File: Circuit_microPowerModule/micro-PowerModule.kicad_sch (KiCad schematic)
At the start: 5 parts, among them Q1 S8550, SW1 RotaryEncoder_Switch, U2 MAX485E

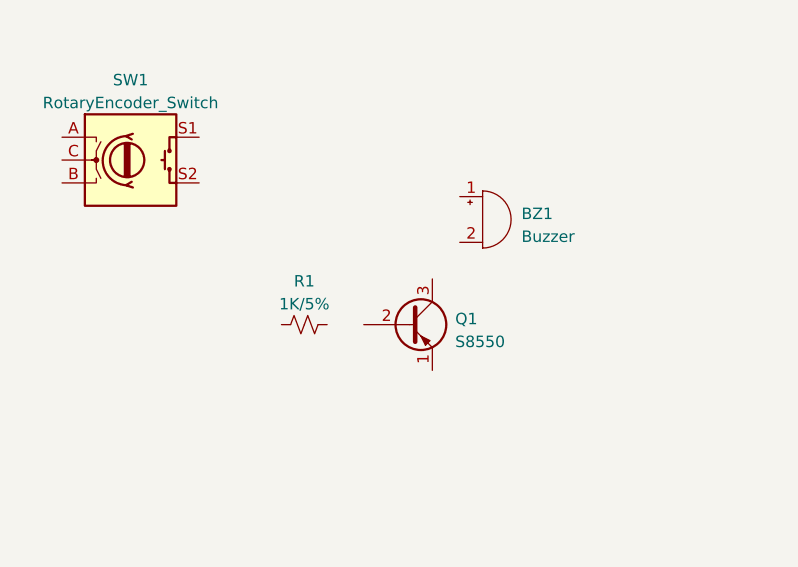
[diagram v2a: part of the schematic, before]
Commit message: new RFQ, update circuit
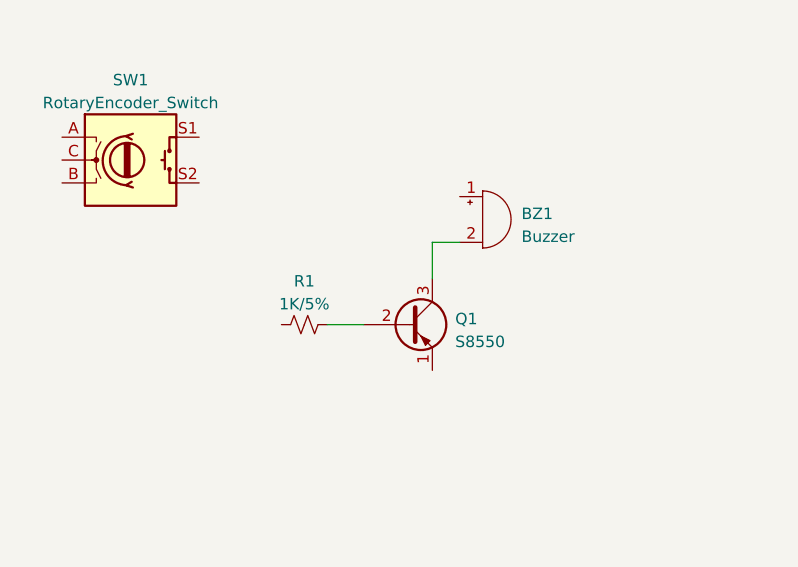
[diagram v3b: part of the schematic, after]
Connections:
- net at Q1.2 (B): now also R1.2
- net at Q1.3 (C): now also BZ1.2 (+)
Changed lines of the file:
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@@
     (rev "0.0")
+  )
+  (wire (pts (xy 98.552 146.304) (xy 98.552 142.24))
+    (stroke (width 0) (type default))
+  )
+  (wire (pts (xy 86.868 151.384) (xy 90.932 151.384))
+    (stroke (width 0) (type default))
+  )
+  (wire (pts (xy 98.552 142.24) (xy 101.6 142.24))
+    (stroke (width 0) (type default))
   )
   (image (at 274.066 161.798) (scale 0.614583)
